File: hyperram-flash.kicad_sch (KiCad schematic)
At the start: 17 parts, among them U1 IS66WVH16M8DBLL-100B1LI, U3 S25FL128SAGNFI000

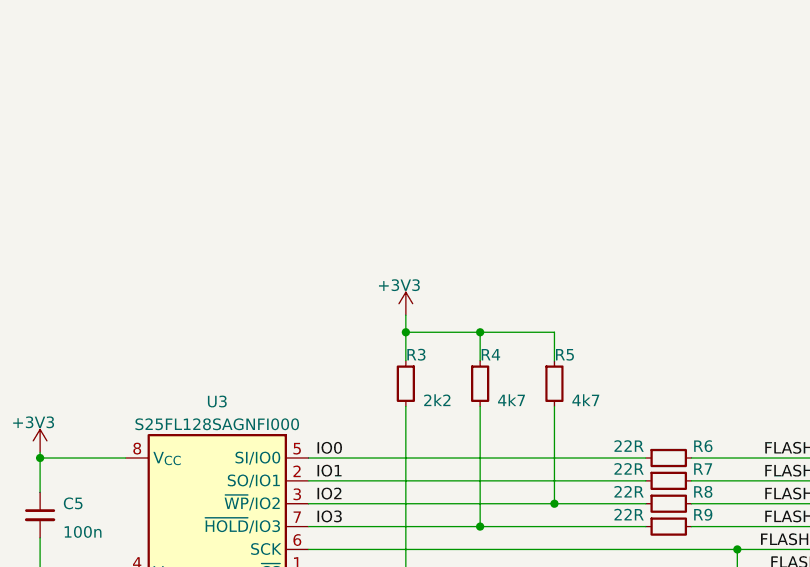
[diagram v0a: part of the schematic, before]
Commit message: [#66311] Add XCAU25P. Reconnect configuration bank 0
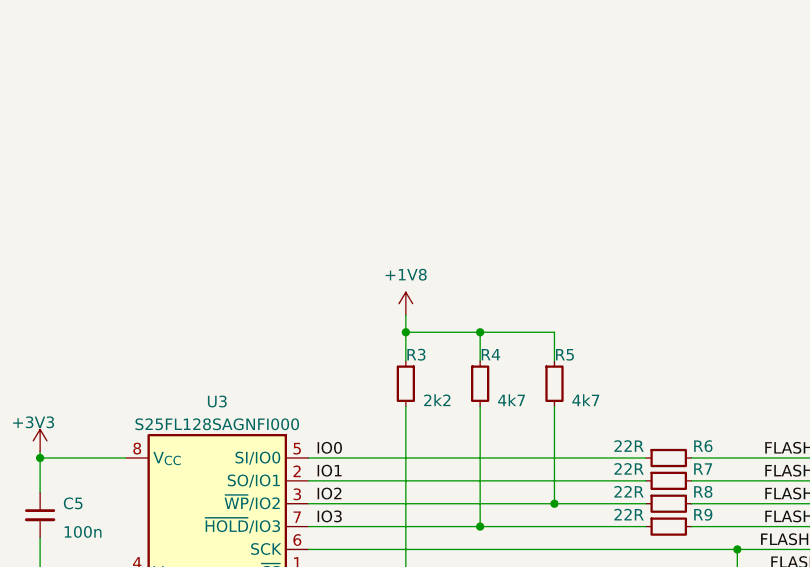
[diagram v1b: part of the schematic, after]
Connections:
- net +3V3: no longer R3.1, R4.1, R5.1
- new net +1V8: R3.1, R4.1, R5.1
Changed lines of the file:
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@@
-    )
-  )
-  (symbol (lib_id "antmicropower:+3V3") (at 210.82 189.865 0) (unit 1)
-    (in_bom yes) (on_board yes) (dnp no)
-    (property "Reference" "#PWR0173" (at 210.82 193.675 0)
-      (effects (font (size 1.27 1.27)) hide)
-    )
-    (property "Value" "+3V3" (at 207.645 187.325 0)
-      (effects (font (size 1.27 1.27) (thickness 0.15)) (justify left bottom))
-    )
-    (property "Footprint" "" (at 226.06 197.485 0)
-      (effects (font (size 1.27 1.27) (thickness 0.15)) (justify left bottom) hide)
-    )
-    (property "Datasheet" "" (at 226.06 200.025 0)
-      (effects (font (size 1.27 1.27) (thickness 0.15)) (justify left bottom) hide)
-    )
-    (property "Author" "Antmicro" (at 226.06 192.405 0)
-      (effects (font (size 1.27 1.27) (thickness 0.15)) (justify left bottom) hide)
-    )
-    (property "License" "Apache-2.0" (at 226.06 194.945 0)
-      (effects (font (size 1.27 1.27) (thickness 0.15)) (justify left bottom) hide)
-    )
-    (pin "1")
-    (instances
-      (project "rdimm-ddr5-tester-ultrascale-plus"
-        (path "/1faa6543-e26a-4449-8bac-ee14b9f19e5f/00000000-0000-0000-0000-00005fea2994"
-          (reference "#PWR0173") (unit 1)
-        )
-      )
     )
   )
@@
         )
       )
+    )
+  )
+  (symbol (lib_id "antmicropower:+1V8") (at 210.82 189.865 0) (unit 1)
+    (in_bom yes) (on_board yes) (dnp no) (fields_autoplaced)
+    (property "Reference" "#PWR024" (at 226.06 192.405 0)
+      (effects (font (size 1.27 1.27) (thickness 0.15)) (justify left bottom) hide)
+    )
+    (property "Value" "+1V8" (at 210.82 185.42 0)
+      (effects (font (size 1.27 1.27) (thickness 0.15)))
+    )
+    (property "Footprint" "" (at 226.06 197.485 0)
+      (effects (font (size 1.27 1.27) (thickness 0.15)) (justify left bottom) hide)
+    )
+    (property "Datasheet" "" (at 226.06 200.025 0)
+      (effects (font (size 1.27 1.27) (thickness 0.15)) (justify left bottom) hide)
+    )
+    (property "Author" "Antmicro" (at 226.06 194.945 0)
+      (effects (font (size 1.27 1.27) (thickness 0.15)) (justify left bottom) hide)
+    )
+    (property "License" "Apache-2.0" (at 226.06 197.485 0)
+      (effects (font (size 1.27 1.27) (thickness 0.15)) (justify left bottom) hide)
+    )
+    (pin "1")
+    (instances
+      (project "rdimm-ddr5-tester-ultrascale-plus"
+        (path "/1faa6543-e26a-4449-8bac-ee14b9f19e5f/00000000-0000-0000-0000-00005fea2994"
+          (reference "#PWR024") (unit 1)
+        )
+      )

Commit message: [#65754] Rename project
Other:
- title: SO-DIMM DDR5 Tester -> RDIMM DDR5 Tester
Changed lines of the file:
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@@
   (paper "A3")
   (title_block
-    (title "SO-DIMM DDR5 Tester")
-    (date "2024-04-23")
-    (rev "1.2.0")
+    (title "RDIMM DDR5 Tester")
+    (date "2024-09-26")
+    (rev "2.0.0")
     (company "Antmicro Ltd.")
     (comment 1 "www.antmicro.com")
@@
     (pin "2")
     (instances
-      (project "rdimm-ddr5-tester-ultrascale-plus"
+      (project "data-center-rdimm-ddr5-tester"
         (path "/1faa6543-e26a-4449-8bac-ee14b9f19e5f/00000000-0000-0000-0000-00005fea2994"
           (reference "C1") (unit 1)
@@
     (pin "2")
     (instances
-      (project "rdimm-ddr5-tester-ultrascale-plus"
+      (project "data-center-rdimm-ddr5-tester"
         (path "/1faa6543-e26a-4449-8bac-ee14b9f19e5f/00000000-0000-0000-0000-00005fea2994"
           (reference "C3") (unit 1)
@@
     (pin "1")
     (instances
-      (project "rdimm-ddr5-tester-ultrascale-plus"
+      (project "data-center-rdimm-ddr5-tester"
         (path "/1faa6543-e26a-4449-8bac-ee14b9f19e5f/00000000-0000-0000-0000-00005fea2994"
           (reference "#PWR04") (unit 1)
@@
     (pin "2")
     (instances
-      (project "rdimm-ddr5-tester-ultrascale-plus"
+      (project "data-center-rdimm-ddr5-tester"
         (path "/1faa6543-e26a-4449-8bac-ee14b9f19e5f/00000000-0000-0000-0000-00005fea2994"
           (reference "R1") (unit 1)
@@
     (pin "1")
     (instances
-      (project "rdimm-ddr5-tester-ultrascale-plus"
+      (project "data-center-rdimm-ddr5-tester"
         (path "/1faa6543-e26a-4449-8bac-ee14b9f19e5f/00000000-0000-0000-0000-00005fea2994"
           (reference "#PWR05") (unit 1)
@@
     (pin "1")
     (instances
-      (project "rdimm-ddr5-tester-ultrascale-plus"
+      (project "data-center-rdimm-ddr5-tester"
         (path "/1faa6543-e26a-4449-8bac-ee14b9f19e5f/00000000-0000-0000-0000-00005fea2994"
           (reference "#PWR06") (unit 1)
@@
     (pin "2")
     (instances
-      (project "rdimm-ddr5-tester-ultrascale-plus"
+      (project "data-center-rdimm-ddr5-tester"
         (path "/1faa6543-e26a-4449-8bac-ee14b9f19e5f/00000000-0000-0000-0000-00005fea2994"
           (reference "C2") (unit 1)
@@
     (pin "2")
     (instances
-      (project "rdimm-ddr5-tester-ultrascale-plus"
+      (project "data-center-rdimm-ddr5-tester"
         (path "/1faa6543-e26a-4449-8bac-ee14b9f19e5f/00000000-0000-0000-0000-00005fea2994"
           (reference "R2") (unit 1)
@@
     (pin "1")
     (instances
-      (project "rdimm-ddr5-tester-ultrascale-plus"
+      (project "data-center-rdimm-ddr5-tester"
         (path "/1faa6543-e26a-4449-8bac-ee14b9f19e5f/00000000-0000-0000-0000-00005fea2994"
           (reference "#PWR03") (unit 1)
@@
     (pin "2")
     (instances
-      (project "rdimm-ddr5-tester-ultrascale-plus"
+      (project "data-center-rdimm-ddr5-tester"
         (path "/1faa6543-e26a-4449-8bac-ee14b9f19e5f/00000000-0000-0000-0000-00005fea2994"
           (reference "C4") (unit 1)
@@
     (pin "1")
     (instances
-      (project "rdimm-ddr5-tester-ultrascale-plus"
+      (project "data-center-rdimm-ddr5-tester"
         (path "/1faa6543-e26a-4449-8bac-ee14b9f19e5f/00000000-0000-0000-0000-00005fea2994"
           (reference "#PWR07") (unit 1)
@@
     (pin "2")
     (instances
-      (project "rdimm-ddr5-tester-ultrascale-plus"
+      (project "data-center-rdimm-ddr5-tester"
         (path "/1faa6543-e26a-4449-8bac-ee14b9f19e5f/00000000-0000-0000-0000-00005fea2994"
           (reference "R7") (unit 1)
@@
     (pin "2")
     (instances
-      (project "rdimm-ddr5-tester-ultrascale-plus"
+      (project "data-center-rdimm-ddr5-tester"
         (path "/1faa6543-e26a-4449-8bac-ee14b9f19e5f/00000000-0000-0000-0000-00005fea2994"
           (reference "R8") (unit 1)
@@
     (pin "2")
     (instances
-      (project "rdimm-ddr5-tester-ultrascale-plus"
+      (project "data-center-rdimm-ddr5-tester"
         (path "/1faa6543-e26a-4449-8bac-ee14b9f19e5f/00000000-0000-0000-0000-00005fea2994"
           (reference "R5") (unit 1)
@@
     (pin "2")
     (instances
-      (project "rdimm-ddr5-tester-ultrascale-plus"
+      (project "data-center-rdimm-ddr5-tester"
         (path "/1faa6543-e26a-4449-8bac-ee14b9f19e5f/00000000-0000-0000-0000-00005fea2994"
           (reference "R9") (unit 1)
@@
     (pin "2")
     (instances
-      (project "rdimm-ddr5-tester-ultrascale-plus"
+      (project "data-center-rdimm-ddr5-tester"
         (path "/1faa6543-e26a-4449-8bac-ee14b9f19e5f/00000000-0000-0000-0000-00005fea2994"
           (reference "C5") (unit 1)
@@
     (pin "1")
     (instances
-      (project "rdimm-ddr5-tester-ultrascale-plus"
+      (project "data-center-rdimm-ddr5-tester"
         (path "/1faa6543-e26a-4449-8bac-ee14b9f19e5f/00000000-0000-0000-0000-00005fea2994"
           (reference "#PWR0172") (unit 1)
@@
     (pin "2")
     (instances
-      (project "rdimm-ddr5-tester-ultrascale-plus"
+      (project "data-center-rdimm-ddr5-tester"
         (path "/1faa6543-e26a-4449-8bac-ee14b9f19e5f/00000000-0000-0000-0000-00005fea2994"
           (reference "R3") (unit 1)
@@
     (pin "2")
     (instances
-      (project "rdimm-ddr5-tester-ultrascale-plus"
+      (project "data-center-rdimm-ddr5-tester"
         (path "/1faa6543-e26a-4449-8bac-ee14b9f19e5f/00000000-0000-0000-0000-00005fea2994"
           (reference "R4") (unit 1)
@@
     (pin "2")
     (instances
-      (project "rdimm-ddr5-tester-ultrascale-plus"
+      (project "data-center-rdimm-ddr5-tester"
         (path "/1faa6543-e26a-4449-8bac-ee14b9f19e5f/00000000-0000-0000-0000-00005fea2994"
           (reference "R6") (unit 1)
@@
     (pin "1")
     (instances
-      (project "rdimm-ddr5-tester-ultrascale-plus"
+      (project "data-center-rdimm-ddr5-tester"
         (path "/1faa6543-e26a-4449-8bac-ee14b9f19e5f/00000000-0000-0000-0000-00005fea2994"
           (reference "#PWR0169") (unit 1)
@@
     (pin "1")
     (instances
-      (project "rdimm-ddr5-tester-ultrascale-plus"
+      (project "data-center-rdimm-ddr5-tester"
         (path "/1faa6543-e26a-4449-8bac-ee14b9f19e5f/00000000-0000-0000-0000-00005fea2994"
           (reference "#PWR01") (unit 1)
@@
     (pin "1")
     (instances
-      (project "rdimm-ddr5-tester-ultrascale-plus"
+      (project "data-center-rdimm-ddr5-tester"
         (path "/1faa6543-e26a-4449-8bac-ee14b9f19e5f/00000000-0000-0000-0000-00005fea2994"
           (reference "#PWR024") (unit 1)
@@
     (pin "1")
     (instances
-      (project "rdimm-ddr5-tester-ultrascale-plus"
+      (project "data-center-rdimm-ddr5-tester"
         (path "/1faa6543-e26a-4449-8bac-ee14b9f19e5f/00000000-0000-0000-0000-00005fea2994"
           (reference "#PWR0170") (unit 1)
@@
     (pin "1")
     (instances
-      (project "rdimm-ddr5-tester-ultrascale-plus"
+      (project "data-center-rdimm-ddr5-tester"
         (path "/1faa6543-e26a-4449-8bac-ee14b9f19e5f/00000000-0000-0000-0000-00005fea2994"
           (reference "#PWR02") (unit 1)
@@
     (pin "1")
     (instances
-      (project "rdimm-ddr5-tester-ultrascale-plus"
+      (project "data-center-rdimm-ddr5-tester"
         (path "/1faa6543-e26a-4449-8bac-ee14b9f19e5f/00000000-0000-0000-0000-00005fea2994"
           (reference "#PWR0171") (unit 1)
@@
     (pin "2")
     (instances
-      (project "rdimm-ddr5-tester-ultrascale-plus"
+      (project "data-center-rdimm-ddr5-tester"
         (path "/1faa6543-e26a-4449-8bac-ee14b9f19e5f/00000000-0000-0000-0000-00005fea2994"
           (reference "R10") (unit 1)
@@
     (pin "9")
     (instances
-      (project "rdimm-ddr5-tester-ultrascale-plus"
+      (project "data-center-rdimm-ddr5-tester"
         (path "/1faa6543-e26a-4449-8bac-ee14b9f19e5f/00000000-0000-0000-0000-00005fea2994"
           (reference "U3") (unit 1)
@@
     (pin "E5")
     (instances
-      (project "rdimm-ddr5-tester-ultrascale-plus"
+      (project "data-center-rdimm-ddr5-tester"
         (path "/1faa6543-e26a-4449-8bac-ee14b9f19e5f/00000000-0000-0000-0000-00005fea2994"
           (reference "U1") (unit 1)

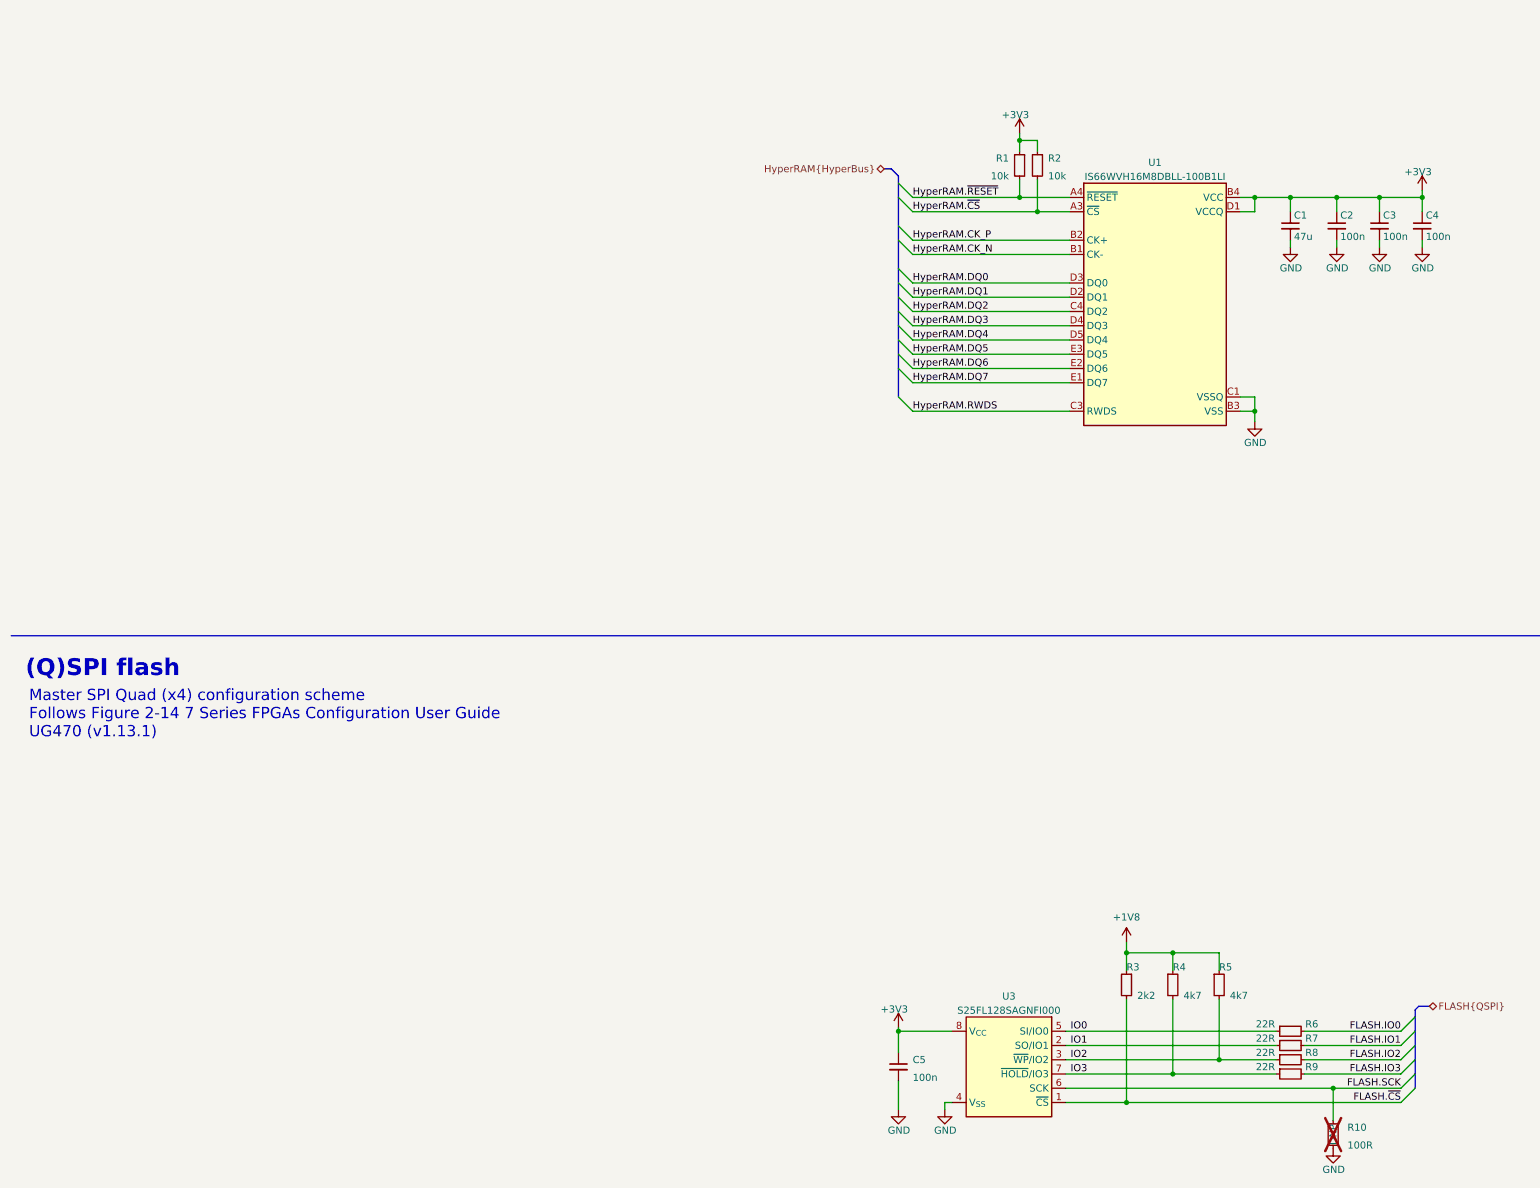
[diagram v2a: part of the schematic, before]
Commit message: [#66311] Replace HyperRam and Flash with 1V8 parts. Add 1V25 ADC VREF for core temp measurement (internal)
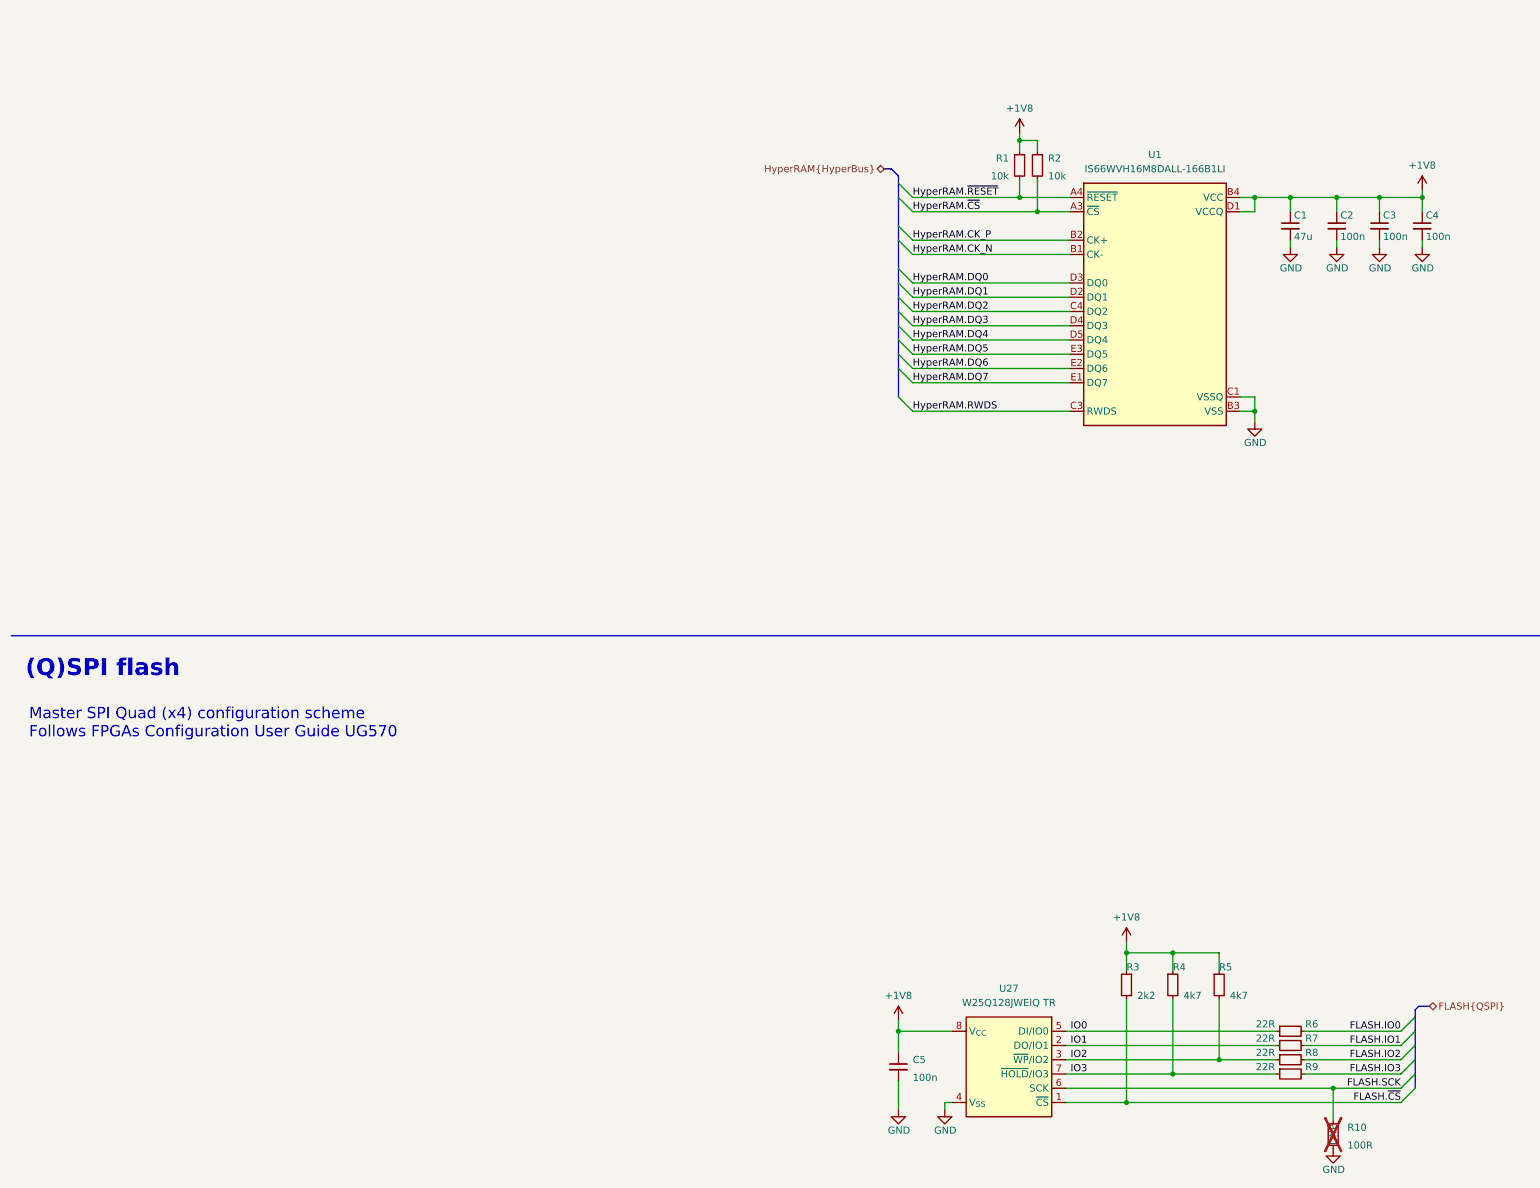
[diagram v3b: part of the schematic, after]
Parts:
- removed U1: IS66WVH16M8DBLL-100B1LI, antmicro-footprints:FBGA-25-24_6x8mm_Layout5x5_P1mm, symbol antmicroMemory:IS66WVH16M8DBLL-100B1LI
- removed U3: S25FL128SAGNFI000, antmicro-footprints:WSON-8_6x8x0.5mm_P1.27mm, symbol antmicroMemory:S25FL128SAGNFI000
- added U1: IS66WVH16M8DALL-166B1LI, antmicro-footprints:FBGA-25-24_6x8mm_Layout5x5_P1mm, symbol antmicroMemory:IS66WVH16M8DALL-166B1LI
- added U27: W25Q128JWEIQ TR, antmicro-footprints:WSON-8_6x8x0.5mm_P1.27mm, symbol antmicroMemory:W25Q128JWEIQ TR
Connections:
- net +3V3 is gone; now on net +1V8: C1.1, C2.1, C3.1, C4.1, C5.1, R1.1, R2.1
- net +1V8: now also U1.B4 (VCC), U1.D1 (VCCQ), U1.E4 (VCCQ), U27.8 (V_{CC})
- net FLASH.SCK: now also U27.6 (SCK)
- net FLASH.~{CS}: now also U27.1 (~{CS})
- net GND: now also U1.B3 (VSS), U1.C1 (VSSQ), U1.E5 (VSSQ), U27.4 (V_{SS})
- net HyperRAM.CK_N: now also U1.B1 (CK-)
- net HyperRAM.CK_P: now also U1.B2 (CK+)
- net HyperRAM.DQ0: now also U1.D3 (DQ0)
- net HyperRAM.DQ1: now also U1.D2 (DQ1)
- net HyperRAM.DQ2: now also U1.C4 (DQ2)
- net HyperRAM.DQ3: now also U1.D4 (DQ3)
- net HyperRAM.DQ4: now also U1.D5 (DQ4)
- net HyperRAM.DQ5: now also U1.E3 (DQ5)
- net HyperRAM.DQ6: now also U1.E2 (DQ6)
- net HyperRAM.DQ7: now also U1.E1 (DQ7)
- net HyperRAM.RWDS: now also U1.C3 (RWDS)
- net HyperRAM.~{CS}: now also U1.A3 (~{CS})
- net HyperRAM.~{RESET}: now also U1.A4 (~{RESET})
- net IO0: now also U27.5 (DI/IO0)
- net IO1: now also U27.2 (DO/IO1)
- net IO2: now also U27.3 (~{WP}/IO2)
- net IO3: now also U27.7 (~{HOLD}/IO3)
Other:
- note added: "Master SPI Quad (x4) configuration scheme Follows FPGAs Configuration User Guide UG570"
- note removed: "Master SPI Quad (x4) configuration scheme Follows Figure 2-14 7 Series FPGAs Configuration User Guide UG470 (v1.13.1)"

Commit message: [#68016] Clean-up the schematic
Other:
- moved on the sheet: C2, C3, C4, C5, R1, R10, R2, R3, R4, R5, R6, R7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
